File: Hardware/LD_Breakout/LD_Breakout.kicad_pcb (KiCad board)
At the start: 2 copper layers, 26.2 x 18.5 mm, 10 parts

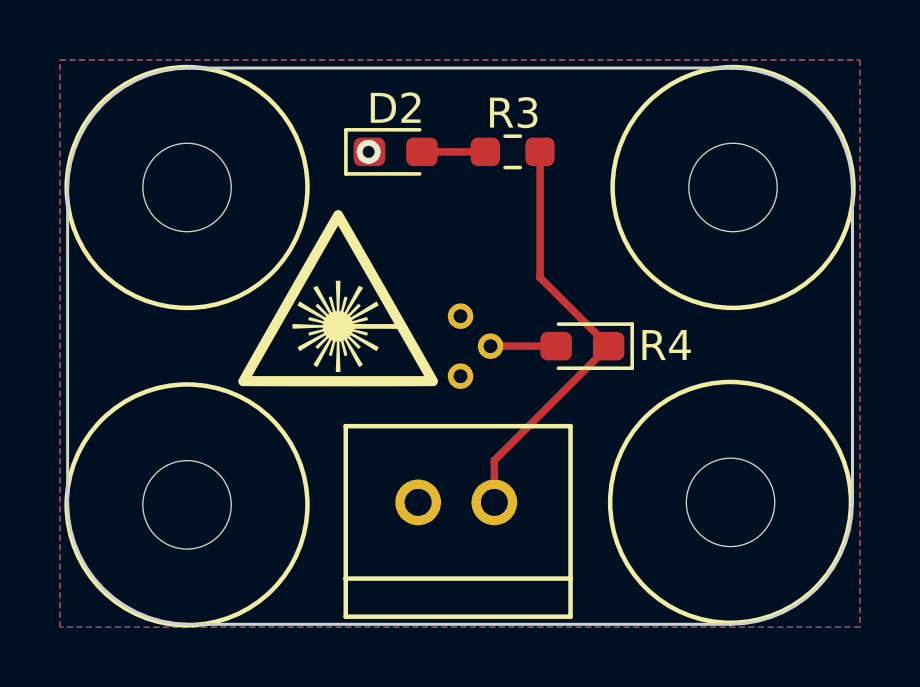
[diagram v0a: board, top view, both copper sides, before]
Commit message: Fixes to LD board
See layout review
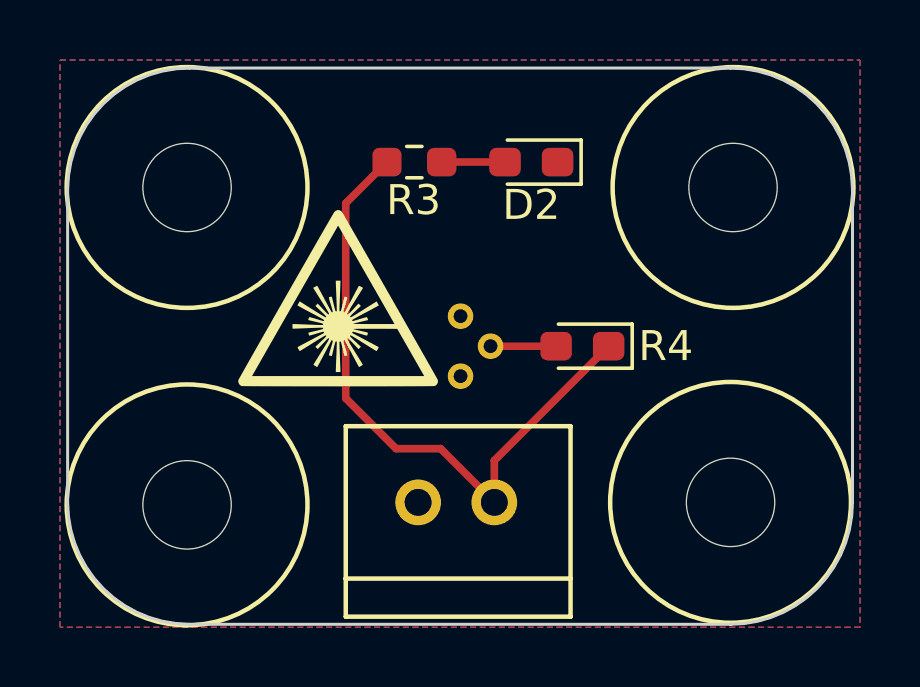
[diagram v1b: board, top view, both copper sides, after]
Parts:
- moved D2 4.53 mm to (134.7, 72.5), turned to 180 degrees
- moved R3 3.30 mm to (130.8, 72.5), turned to 0 degrees
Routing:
- net +5V: track 14.2 -> 21.6 mm
- net GND: vias 1 -> 0
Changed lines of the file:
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@@
   )
   (footprint "Resistor_SMD:R_0603_1608Metric_Pad0.98x0.95mm_HandSolder" (layer "F.Cu")
-    (at 134.0885 72.15 180)
+    (at 130.81 72.4916)
     (descr "Resistor SMD 0603 (1608 Metric), square (rectangular) end terminal, IPC_7351 nominal with elongated pad for handsoldering. (Body size source: IPC-SM-782 page 72, https://www.pcb-3d.com/wordpress/wp-content/uploads/ipc-sm-782a_amendment_1_and_2.pdf), generated with kicad-footprint-generator")
     (tags "resistor handsolder")
@@
     (fp_line (start 0.8 0.4125) (end -0.8 0.4125)
       (stroke (width 0.1) (type solid)) (layer "F.Fab"))
-    (pad "1" smd roundrect (at -0.9125 0 180) (size 0.975 0.95) (layers "F.Cu" "F.Paste" "F.Mask") (roundrect_rratio 0.25)
+    (pad "1" smd roundrect (at -0.9125 0) (size 0.975 0.95) (layers "F.Cu" "F.Paste" "F.Mask") (roundrect_rratio 0.25)
       (net 1 "+5V") (pintype "passive"))
-    (pad "2" smd roundrect (at 0.9125 0 180) (size 0.975 0.95) (layers "F.Cu" "F.Paste" "F.Mask") (roundrect_rratio 0.25)
+    (pad "2" smd roundrect (at 0.9125 0) (size 0.975 0.95) (layers "F.Cu" "F.Paste" "F.Mask") (roundrect_rratio 0.25)
       (net 3 "Net-(D2-A)") (pintype "passive"))
     (model "${KICAD6_3DMODEL_DIR}/Resistor_SMD.3dshapes/R_0603_1608Metric.wrl"
@@
   )
   (footprint "LED_SMD:LED_0603_1608Metric_Pad1.05x0.95mm_HandSolder" (layer "F.Cu")
-    (at 130.189 72.15)
+    (at 134.7095 72.4916 180)
     (descr "LED SMD 0603 (1608 Metric), square (rectangular) end terminal, IPC_7351 nominal, (Body size source: http://www.tortai-tech.com/upload/download/2011102023233369053.pdf), generated with kicad-footprint-generator")
     (tags "LED handsolder")
@@
     (fp_line (start 0.8 0.4) (end 0.8 -0.4)
       (stroke (width 0.1) (type solid)) (layer "F.Fab"))
-    (pad "1" smd roundrect (at -0.875 0) (size 1.05 0.95) (layers "F.Cu" "F.Paste" "F.Mask") (roundrect_rratio 0.25)
+    (pad "1" smd roundrect (at -0.875 0 180) (size 1.05 0.95) (layers "F.Cu" "F.Paste" "F.Mask") (roundrect_rratio 0.25)
       (net 2 "GND") (pinfunction "K") (pintype "passive"))
-    (pad "2" smd roundrect (at 0.875 0) (size 1.05 0.95) (layers "F.Cu" "F.Paste" "F.Mask") (roundrect_rratio 0.25)
+    (pad "2" smd roundrect (at 0.875 0 180) (size 1.05 0.95) (layers "F.Cu" "F.Paste" "F.Mask") (roundrect_rratio 0.25)
       (net 3 "Net-(D2-A)") (pinfunction "A") (pintype "passive"))
     (model "${KICAD6_3DMODEL_DIR}/LED_SMD.3dshapes/LED_0603_1608Metric.wrl"
@@
   (gr_line (start 141.351 87.898) (end 123.317 87.898)
     (stroke (width 0.1) (type default)) (layer "Edge.Cuts"))
-  (segment (start 133.477 82.437) (end 137.287 78.627) (width 0.25) (layer "F.Cu") (net 1))
-  (segment (start 135.001 76.341) (end 135.001 72.15) (width 0.25) (layer "F.Cu") (net 1))
-  (segment (start 133.477 83.834) (end 133.477 82.437) (width 0.25) (layer "F.Cu") (net 1))
-  (segment (start 137.287 78.627) (end 135.001 76.341) (width 0.25) (layer "F.Cu") (net 1))
-  (via (at 129.286 72.15) (size 0.8) (drill 0.4) (layers "F.Cu" "B.Cu") (net 2))
-  (segment (start 133.176 72.15) (end 131.064 72.15) (width 0.25) (layer "F.Cu") (net 3))
-  (segment (start 135.537 78.627) (end 133.35 78.627) (width 0.25) (layer "F.Cu") (net 4))
+  (segment (start 133.477 82.437) (end 137.287 78.627) (width 0.254) (layer "F.Cu") (net 1))
+  (segment (start 131.685 82.042) (end 130.2004 82.042) (width 0.254) (layer "F.Cu") (net 1))
+  (segment (start 130.2004 82.042) (end 128.524 80.3656) (width 0.254) (layer "F.Cu") (net 1))
+  (segment (start 128.524 73.8651) (end 129.8975 72.4916) (width 0.254) (layer "F.Cu") (net 1))
+  (segment (start 133.477 83.834) (end 133.477 82.437) (width 0.254) (layer "F.Cu") (net 1))
+  (segment (start 128.524 80.3656) (end 128.524 73.8651) (width 0.254) (layer "F.Cu") (net 1))
+  (segment (start 133.477 83.834) (end 131.685 82.042) (width 0.254) (layer "F.Cu") (net 1))
+  (segment (start 131.7225 72.4916) (end 133.8345 72.4916) (width 0.254) (layer "F.Cu") (net 3))
+  (segment (start 135.537 78.627) (end 133.35 78.627) (width 0.254) (layer "F.Cu") (net 4))
   (zone (net 2) (net_name "GND") (layers "F&B.Cu") (name "GND") (hatch edge 0.5)
     (priority 1)

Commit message: Added Labels
should be ready for a board review?
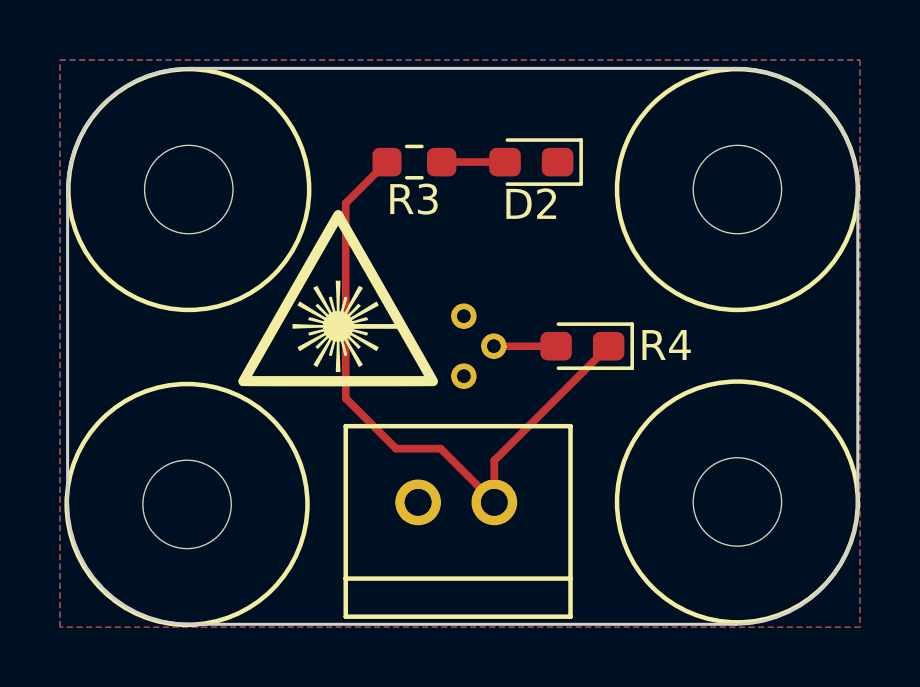
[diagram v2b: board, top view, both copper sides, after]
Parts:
- moved H3 0.23 mm to (137.6, 79.8)
- moved H2 0.16 mm to (137.6, 77.4)
- moved LD2 0.11 mm to (132.5, 78.6)
- moved H1 0.09 mm to (127.3, 77.4)
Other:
- board size 26.2 x 18.5 mm -> 26.3 x 18.5 mm
- board text added: "LD Breakout, Rev1, MRDT, MS&T, 2023"
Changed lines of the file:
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@@
   )
   (footprint "MRDT_Drill_Holes:4_40_Hole_Corner" (layer "F.Cu")
-    (at 127.2427 79.9083 180)
+    (at 127.2427 79.8943 180)
     (property "Sheetfile" "LD_Breakout.kicad_sch")
     (property "Sheetname" "")
@@
   )
   (footprint "MRDT_Drill_Holes:4_40_Hole_Corner" (layer "F.Cu")
-    (at 127.2427 77.3457 90)
+    (at 127.29972 77.41412 90)
     (property "Sheetfile" "LD_Breakout.kicad_sch")
     (property "Sheetname" "")
@@
   )
   (footprint "MRDT_Drill_Holes:4_40_Hole_Corner" (layer "F.Cu")
-    (at 137.34288 79.82588 -90)
+    (at 137.57148 79.81188 -90)
     (property "Sheetfile" "LD_Breakout.kicad_sch")
     (property "Sheetname" "")
@@
   )
   (footprint "MRDT_Drill_Holes:4_40_Hole_Corner" (layer "F.Cu")
-    (at 137.4253 77.3457)
+    (at 137.57148 77.41412)
     (property "Sheetfile" "LD_Breakout.kicad_sch")
     (property "Sheetname" "")
@@
   )
   (footprint "FTIR_Footprints:RLD63NPC5" (layer "B.Cu")
-    (at 132.35 78.627 180)
+    (at 132.461 78.627 180)
     (property "Sheetfile" "LD_Breakout.kicad_sch")
     (property "Sheetname" "")
@@
     (property "ki_keywords" "opto laserdiode photodiode")
     (attr smd)
-    (fp_text reference "LD2" (at 0 7.6 unlocked) (layer "B.SilkS")
+    (fp_text reference "LD2" (at 4.8514 -0.0622 unlocked) (layer "B.SilkS")
         (effects (font (size 1 1) (thickness 0.1)) (justify mirror))
     )
@@
       (net 5 "unconnected-(LD2-Pad3)") (pintype "passive+no_connect"))
   )
-  (gr_rect (start 123.317 73.42) (end 132.334 78.627)
+  (gr_rect (start 123.317 73.42) (end 132.461 78.627)
     (stroke (width 0.1) (type default)) (fill none) (layer "Dwgs.User"))
-  (gr_rect (start 123.317 73.42) (end 141.351 83.834)
+  (gr_rect (start 123.317 73.42) (end 141.605 83.834)
     (stroke (width 0.15) (type default)) (fill none) (layer "Dwgs.User"))
-  (gr_line (start 119.253 73.42) (end 119.253 83.834)
-    (stroke (width 0.1) (type default)) (layer "Edge.Cuts"))
-  (gr_line (start 145.415 83.834) (end 145.415 73.42)
-    (stroke (width 0.1) (type default)) (layer "Edge.Cuts"))
   (gr_arc (start 123.317 87.898) (mid 120.443318 86.707682) (end 119.253 83.834)
     (stroke (width 0.1) (type default)) (layer "Edge.Cuts"))
-  (gr_arc (start 119.253 73.42) (mid 120.443318 70.546318) (end 123.317 69.356)
+  (gr_arc (start 119.253 73.4314) (mid 120.443318 70.557718) (end 123.317 69.3674)
     (stroke (width 0.1) (type default)) (layer "Edge.Cuts"))
-  (gr_arc (start 145.415 83.834) (mid 144.224682 86.707682) (end 141.351 87.898)
+  (gr_line (start 145.5928 83.834) (end 145.5928 73.4314)
     (stroke (width 0.1) (type default)) (layer "Edge.Cuts"))
-  (gr_arc (start 141.351 69.356) (mid 144.224682 70.546318) (end 145.415 73.42)
+  (gr_arc (start 145.5928 83.834) (mid 144.402482 86.707682) (end 141.5288 87.898)
     (stroke (width 0.1) (type default)) (layer "Edge.Cuts"))
-  (gr_line (start 141.351 69.356) (end 123.317 69.356)
+  (gr_arc (start 141.5288 69.3674) (mid 144.402482 70.557718) (end 145.5928 73.4314)
     (stroke (width 0.1) (type default)) (layer "Edge.Cuts"))
-  (gr_line (start 141.351 87.898) (end 123.317 87.898)
+  (gr_line (start 141.5288 87.898) (end 123.317 87.898)
     (stroke (width 0.1) (type default)) (layer "Edge.Cuts"))
+  (gr_line (start 119.253 73.4314) (end 119.253 83.834)
+    (stroke (width 0.1) (type default)) (layer "Edge.Cuts"))
+  (gr_line (start 141.5288 69.3674) (end 123.317 69.3674)
+    (stroke (width 0.1) (type default)) (layer "Edge.Cuts"))
+  (gr_text "LD Breakout, \nRev1, MRDT, \nMS&T, 2023\n" (at 137.16 75.0316) (layer "B.SilkS")
+    (effects (font (size 1 1) (thickness 0.15)) (justify left bottom mirror))
+  )
   (segment (start 133.477 82.437) (end 137.287 78.627) (width 0.254) (layer "F.Cu") (net 1))
   (segment (start 131.685 82.042) (end 130.2004 82.042) (width 0.254) (layer "F.Cu") (net 1))
@@
   (segment (start 133.477 83.834) (end 131.685 82.042) (width 0.254) (layer "F.Cu") (net 1))
   (segment (start 131.7225 72.4916) (end 133.8345 72.4916) (width 0.254) (layer "F.Cu") (net 3))
-  (segment (start 135.537 78.627) (end 133.35 78.627) (width 0.254) (layer "F.Cu") (net 4))
+  (segment (start 135.537 78.627) (end 133.461 78.627) (width 0.254) (layer "F.Cu") (net 4))
   (zone (net 2) (net_name "GND") (layers "F&B.Cu") (name "GND") (hatch edge 0.5)
     (priority 1)

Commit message: Fixed footprints
Some resistors still had LED footprints which I had thought I had fixed, but failed because I did not also update the schematic.
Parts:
- R4: footprint LED_SMD:LED_0603_1608Metric_Pad1.05x0.95mm_HandSolder -> Resistor_SMD:R_0603_1608Metric_Pad0.98x0.95mm_HandSolder
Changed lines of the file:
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@@
     )
   )
-  (footprint "LED_SMD:LED_0603_1608Metric_Pad1.05x0.95mm_HandSolder" (layer "F.Cu")
+  (footprint "Resistor_SMD:R_0603_1608Metric_Pad0.98x0.95mm_HandSolder" (layer "F.Cu")
     (at 136.412 78.627 180)
-    (descr "LED SMD 0603 (1608 Metric), square (rectangular) end terminal, IPC_7351 nominal, (Body size source: http://www.tortai-tech.com/upload/download/2011102023233369053.pdf), generated with kicad-footprint-generator")
-    (tags "LED handsolder")
+    (descr "Resistor SMD 0603 (1608 Metric), square (rectangular) end terminal, IPC_7351 nominal with elongated pad for handsoldering. (Body size source: IPC-SM-782 page 72, https://www.pcb-3d.com/wordpress/wp-content/uploads/ipc-sm-782a_amendment_1_and_2.pdf), generated with kicad-footprint-generator")
+    (tags "resistor handsolder")
     (property "Sheetfile" "LD_Breakout.kicad_sch")
     (property "Sheetname" "")
@@
     (property "ki_keywords" "R res resistor")
     (attr smd)
-    (fp_text reference "R4" (at -2.78 0) (layer "F.SilkS")
+    (fp_text reference "R4" (at 0 1.411 180) (layer "F.SilkS")
         (effects (font (size 1 1) (thickness 0.15)))
     )
-    (fp_text value "85" (at 0 1.43) (layer "F.Fab")
+    (fp_text value "85" (at 0 -1.637 180) (layer "F.Fab")
         (effects (font (size 1 1) (thickness 0.15)))
     )
-    (fp_text user "${REFERENCE}" (at 0 0) (layer "F.Fab")
+    (fp_text user "${REFERENCE}" (at 0 0 180) (layer "F.Fab")
         (effects (font (size 0.4 0.4) (thickness 0.06)))
     )
-    (fp_line (start -1.66 -0.735) (end -1.66 0.735)
+    (fp_line (start -0.254724 -0.5225) (end 0.254724 -0.5225)
       (stroke (width 0.12) (type solid)) (layer "F.SilkS"))
-    (fp_line (start -1.66 0.735) (end 0.8 0.735)
-      (stroke (width 0.12) (type solid)) (layer "F.SilkS"))
-    (fp_line (start 0.8 -0.735) (end -1.66 -0.735)
+    (fp_line (start -0.254724 0.5225) (end 0.254724 0.5225)
       (stroke (width 0.12) (type solid)) (layer "F.SilkS"))
     (fp_line (start -1.65 -0.73) (end 1.65 -0.73)
@@
     (fp_line (start 1.65 0.73) (end -1.65 0.73)
       (stroke (width 0.05) (type solid)) (layer "F.CrtYd"))
-    (fp_line (start -0.8 -0.1) (end -0.8 0.4)
+    (fp_line (start -0.8 -0.4125) (end 0.8 -0.4125)
       (stroke (width 0.1) (type solid)) (layer "F.Fab"))
-    (fp_line (start -0.8 0.4) (end 0.8 0.4)
+    (fp_line (start -0.8 0.4125) (end -0.8 -0.4125)
       (stroke (width 0.1) (type solid)) (layer "F.Fab"))
-    (fp_line (start -0.5 -0.4) (end -0.8 -0.1)
+    (fp_line (start 0.8 -0.4125) (end 0.8 0.4125)
       (stroke (width 0.1) (type solid)) (layer "F.Fab"))
-    (fp_line (start 0.8 -0.4) (end -0.5 -0.4)
+    (fp_line (start 0.8 0.4125) (end -0.8 0.4125)
       (stroke (width 0.1) (type solid)) (layer "F.Fab"))
-    (fp_line (start 0.8 0.4) (end 0.8 -0.4)
-      (stroke (width 0.1) (type solid)) (layer "F.Fab"))
-    (pad "1" smd roundrect (at -0.875 0 180) (size 1.05 0.95) (layers "F.Cu" "F.Paste" "F.Mask") (roundrect_rratio 0.25)
+    (pad "1" smd roundrect (at -0.9125 0 180) (size 0.975 0.95) (layers "F.Cu" "F.Paste" "F.Mask") (roundrect_rratio 0.25)
       (net 1 "+5V") (pintype "passive"))
-    (pad "2" smd roundrect (at 0.875 0 180) (size 1.05 0.95) (layers "F.Cu" "F.Paste" "F.Mask") (roundrect_rratio 0.25)
+    (pad "2" smd roundrect (at 0.9125 0 180) (size 0.975 0.95) (layers "F.Cu" "F.Paste" "F.Mask") (roundrect_rratio 0.25)
       (net 4 "Net-(LD2-Pad2)") (pintype "passive"))
-    (model "${KICAD6_3DMODEL_DIR}/LED_SMD.3dshapes/LED_0603_1608Metric.wrl"
+    (model "${KICAD6_3DMODEL_DIR}/Resistor_SMD.3dshapes/R_0603_1608Metric.wrl"
       (offset (xyz 0 0 0))
       (scale (xyz 1 1 1))

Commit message: Fixed 68 errors
It works now hopefully?
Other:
- board text added: "Laser Diode Breakout, Rev1 Mars Rover Design Team Missouri S&T, 2023"
- board text removed: "LD Breakout, Rev1, MRDT, MS&T, 2023"
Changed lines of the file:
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@@
   (gr_line (start 141.5288 69.3674) (end 123.317 69.3674)
     (stroke (width 0.1) (type default)) (layer "Edge.Cuts"))
-  (gr_text "LD Breakout, \nRev1, MRDT, \nMS&T, 2023\n" (at 137.16 75.0316) (layer "B.SilkS")
-    (effects (font (size 1 1) (thickness 0.15)) (justify left bottom mirror))
+  (gr_text "Laser Diode Breakout, Rev1\nMars Rover Design Team \nMissouri S&T, 2023" (at 136.7028 74.8792) (layer "B.SilkS")
+    (effects (font (size 1.016 0.4318) (thickness 0.09525) bold) (justify left bottom mirror))
   )
   (segment (start 133.477 82.437) (end 137.287 78.627) (width 0.254) (layer "F.Cu") (net 1))

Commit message: Added names to mini boards
Drew told me to
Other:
- board text added: "Drew W. Adam K."
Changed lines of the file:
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@@
   (gr_line (start 141.5288 69.3674) (end 123.317 69.3674)
     (stroke (width 0.1) (type default)) (layer "Edge.Cuts"))
+  (gr_text "Drew W.\nAdam K." (at 137.0076 86.9188) (layer "B.SilkS")
+    (effects (font (size 0.635 0.635) (thickness 0.15)) (justify left bottom mirror))
+  )
   (gr_text "Laser Diode Breakout, Rev1\nMars Rover Design Team \nMissouri S&T, 2023" (at 136.7028 74.8792) (layer "B.SilkS")
     (effects (font (size 1.016 0.4318) (thickness 0.09525) bold) (justify left bottom mirror))
